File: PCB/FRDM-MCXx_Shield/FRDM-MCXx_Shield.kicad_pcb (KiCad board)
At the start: 4 copper layers, 91.4 x 54.6 mm, 92 parts, among them J2 Barrel_Jack_Switch, J3 Conn_01x04_Socket, J4 Conn_01x05_Socket, J5 Conn_01x06_Socket, M1 Motor_Servo, Q1 IRLML6401, SW1 PEC11L-4120F-N0020, SW2 SW_Push, U1 M95010-RMN6TP, U2 FXLS8974CF, U3 SHT31A-DIS, U5 SN74LV164ADR

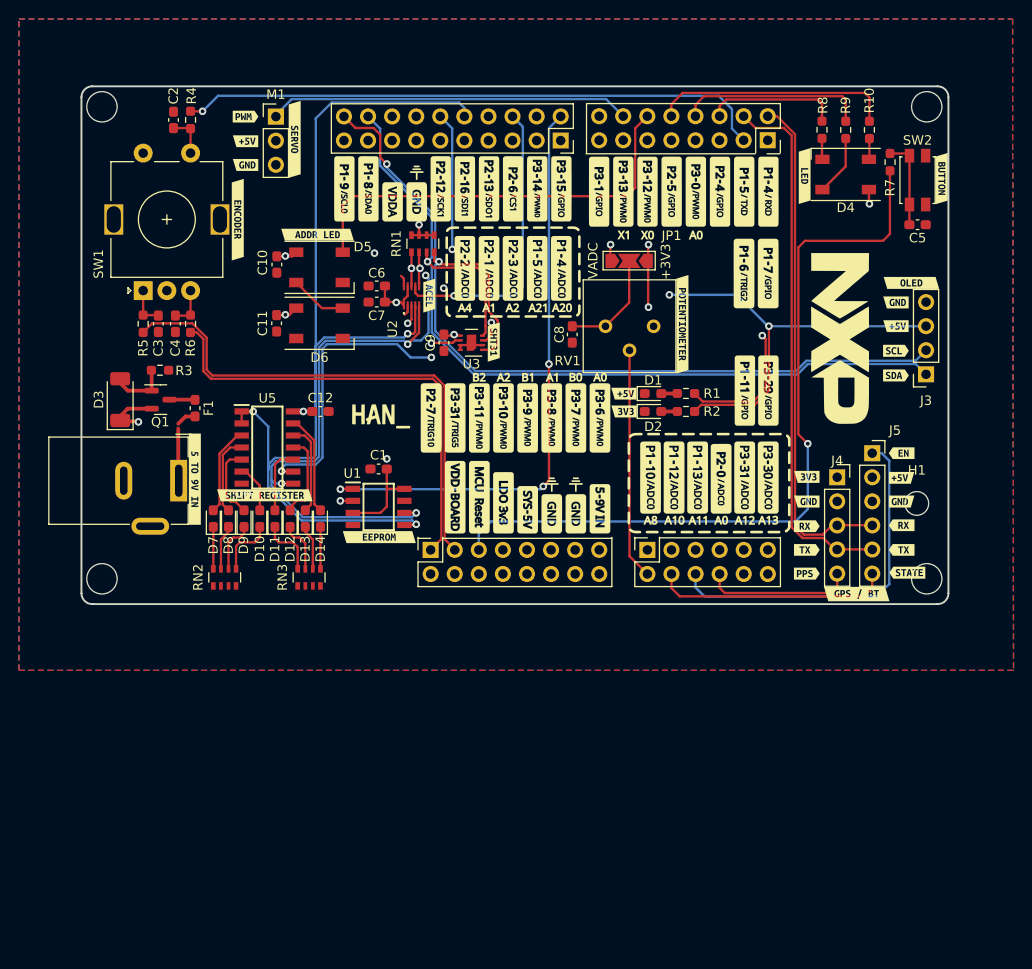
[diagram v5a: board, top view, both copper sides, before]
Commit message: Updated schematic and PCB
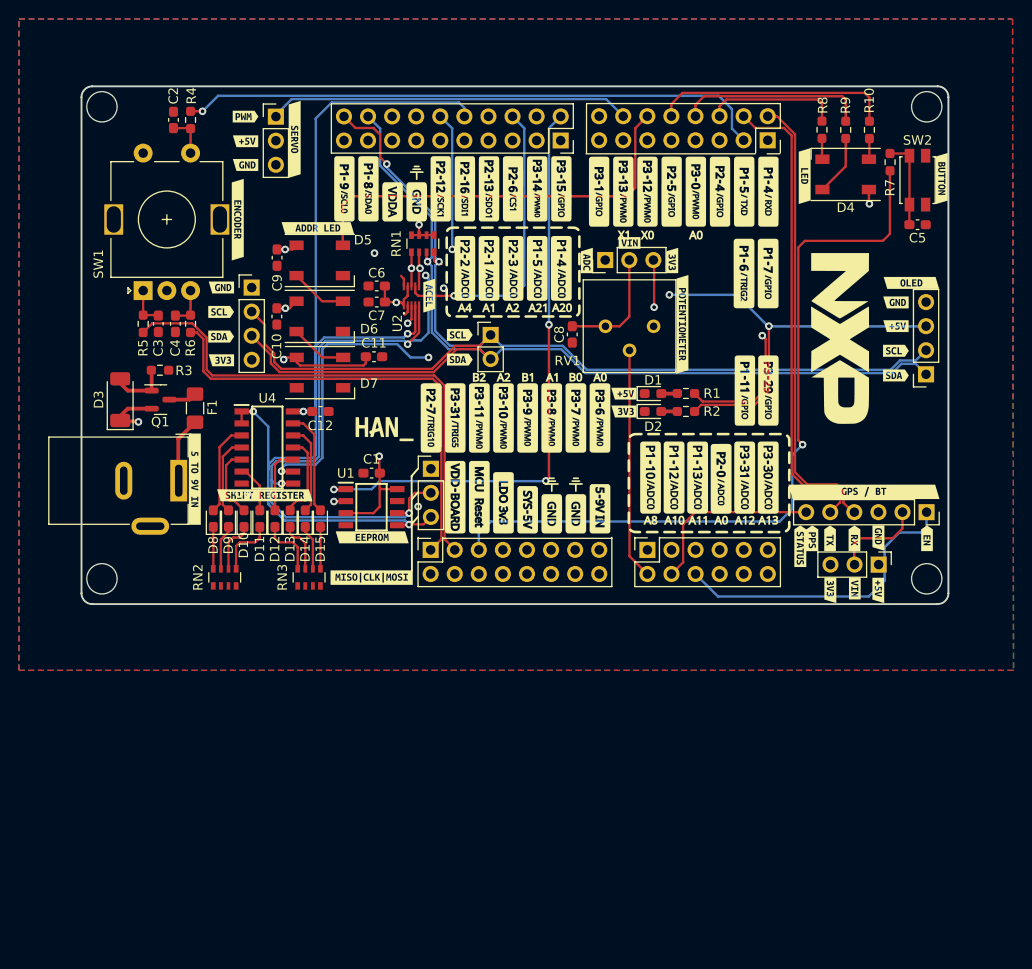
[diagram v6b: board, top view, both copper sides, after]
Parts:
- removed the C9 at (142.4, 86.2)
- removed H1: MountingHole, MountingHole:MountingHole_2.5mm
- removed U3: SHT31A-DIS, Sensor_Humidity:Sensirion_DFN-8-1EP_2.5x2.5mm_P0.5mm_EP1.1x1.7mm
- removed kibuzzard-65C7C4BF: G***, kibuzzard-65C7C4BF
- removed kibuzzard-65C7C4D7: G***, kibuzzard-65C7C4D7
- removed kibuzzard-65C7C4F7: G***, kibuzzard-65C7C4F7
- removed kibuzzard-65C7C50F: G***, kibuzzard-65C7C50F
- removed kibuzzard-65C7C529: G***, kibuzzard-65C7C529
- removed kibuzzard-65C7C54F: G***, kibuzzard-65C7C54F
- removed kibuzzard-65C7C588: G***, kibuzzard-65C7C588
- removed kibuzzard-65C7C594: G***, kibuzzard-65C7C594
- removed the kibuzzard-65C7C5A7 at (180.7, 102.9)
- removed kibuzzard-65C7C5B4: G***, kibuzzard-65C7C5B4
- removed kibuzzard-65C7CC57: G***, kibuzzard-65C7CC57
- removed kibuzzard-65C7CCCF: G***, kibuzzard-65C7CCCF
- added C11: 100nF, Capacitor_SMD:C_0603_1608Metric_Pad1.08x0.95mm_HandSolder, F.Cu at (135.1, 87.6)
- added D7: SK6812, LED_SMD:LED_SK6812_PLCC4_5.0x5.0mm_P3.2mm, F.Cu at (129.3, 89.3)
- added J2: Conn_01x03_Pin, Connector_PinHeader_2.54mm:PinHeader_1x03_P2.54mm_Vertical, F.Cu at (141.1, 99.4)
- added J3: Conn_01x02_Pin, Connector_PinHeader_2.54mm:PinHeader_1x02_P2.54mm_Vertical, F.Cu at (147.3, 85.3)
- added JP2: SolderJumper_3_Open, Connector_PinHeader_2.54mm:PinHeader_1x03_P2.54mm_Vertical, F.Cu at (188.3, 109.5)
- added kibuzzard-65C7C751: G***, kibuzzard-65C7C751, F.Cu at (118.9, 82.9)
- added kibuzzard-65C7C751: G***, kibuzzard-65C7C751, F.Cu at (144.1, 85.3)
- added kibuzzard-65C7C77A: G***, kibuzzard-65C7C77A, F.Cu at (144.1, 87.9)
- added kibuzzard-65C7C77A: G***, kibuzzard-65C7C77A, F.Cu at (118.9, 85.5)
- added kibuzzard-65D5B8C7: G***, kibuzzard-65D5B8C7, F.Cu at (188.2, 106.8)
- added kibuzzard-65D5B8D9: G***, kibuzzard-65D5B8D9, F.Cu at (185.7, 106.8)
- added kibuzzard-65D5B8E6: G***, kibuzzard-65D5B8E6, F.Cu at (183.2, 106.8)
- added kibuzzard-65D5B934: G***, kibuzzard-65D5B934, F.Cu at (183.2, 112.3)
- added kibuzzard-65D5B943: G***, kibuzzard-65D5B943, F.Cu at (188.2, 112.3)
- added kibuzzard-65D5B980: G***, kibuzzard-65D5B980, F.Cu at (181.3, 106.8)
- added kibuzzard-65D5B9E2: G***, kibuzzard-65D5B9E2, F.Cu at (185.8, 112.1)
- added kibuzzard-65D5B9E2: G***, kibuzzard-65D5B9E2, F.Cu at (162.0, 75.6)
- added kibuzzard-65D5C5A7: G***, kibuzzard-65D5C5A7, F.Cu at (180.0, 107.6)
- added kibuzzard-65D5C7B2: G***, kibuzzard-65D5C7B2, F.Cu at (119.0, 88.0)
- added kibuzzard-65D5C7BA: G***, kibuzzard-65D5C7BA, F.Cu at (119.0, 80.3)
- added kibuzzard-65D5C99D: G***, kibuzzard-65D5C99D, F.Cu at (186.7, 101.9)
- added kibuzzard-65D5CAF7: G***, kibuzzard-65D5CAF7, F.Cu at (166.5, 77.5)
- added kibuzzard-65D5CB13: G***, kibuzzard-65D5CB13, F.Cu at (157.5, 77.5)
- added kibuzzard-65D5CBEE: G***, kibuzzard-65D5CBEE, F.Cu at (134.8, 110.9)
- F1: footprint Fuse:Fuse_0603_1608Metric_Pad1.05x0.95mm_HandSolder -> Fuse:Fuse_1206_3216Metric_Pad1.42x1.75mm_HandSolder
- J4: value Conn_01x05_Socket -> Conn_01x04_Pin; footprint Connector_PinSocket_2.54mm:PinSocket_1x05_P2.54mm_Vertical -> Connector_PinHeader_2.54mm:PinHeader_1x04_P2.54mm_Vertical
- JP1: footprint Jumper:SolderJumper-3_P2.0mm_Open_TrianglePad1.0x1.5mm_NumberLabels -> Connector_PinHeader_2.54mm:PinHeader_1x03_P2.54mm_Vertical
- moved J4 64.9 mm to (122.2, 80.3)
- moved kibuzzard-65C7C6CC 9.37 mm to (193.4, 106.8), turned to -90 degrees
- moved J7 8.46 mm to (193.3, 104.0), turned to -90 degrees
- moved JP1 2.53 mm to (159.4, 77.4), turned to 90 degrees
- moved G*** 1.39 mm to (136.2, 95.2)
- moved C1 0.85 mm to (134.8, 99.9)
- moved U1 0.75 mm to (134.8, 103.5)
- moved kibuzzard-65C7CB3C 0.75 mm to (134.9, 106.7)
- moved C9 0.73 mm to (124.8, 77.2)
- moved D5 0.73 mm to (129.3, 77.5)
- moved C10 0.73 mm to (124.8, 83.4)
- moved D6 0.73 mm to (129.3, 83.4)
- moved kibuzzard-65C7CE88 0.70 mm to (129.1, 74.0)
- renumbered C11 to C10, C10 to C9, D9 to D10, D10 to D11, D11 to D12, D12 to D13, D13 to D14, D14 to D15, D7 to D8, D8 to D9, J2 to J5, J3 to J6, J5 to J7, U5 to U4
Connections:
- net /BT_STATE renamed /BT_STATE/GPS_PPS
- D6 pad 4: unconnected-(D6-DOUT-Pad4) -> Net-(D6-DOUT)
- J1 pad B7: /TEMP_ALERT -> unconnected-(J1B-P2-1/ADC0-A1-PadB7)
- J1 pad B9: /~{TEMP_RST} -> unconnected-(J1B-P2-2/ADC0-A4-PadB9)
- J1 pad C8: /GPS_PPS -> unconnected-(J1C-P2-0/ADC0-A0-PadC8)
- J4 pad 1: +3.3V -> GND
- J4 pad 2: GND -> /SCL
- J4 pad 3: /RX -> /SDA
- J4 pad 4: /TX -> +3.3V
- J7 pad 2: +5V -> Net-(J7-Pin_2)
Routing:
- net /~{TEMP_RST}: track 30.3 -> 0.00 mm, vias 1 -> 0
- net /TEMP_ALERT: track 23.4 -> 0.00 mm, vias 1 -> 0
- net +5V: track 168.7 -> 188.9 mm
- net /SCL: track 99.4 -> 116.1 mm
- net /SDA: track 95.2 -> 111.5 mm
- net /GPS_PPS: track 15.8 -> 0.00 mm
- net Net-(J7-Pin_2): track 0.00 -> 9.68 mm
- net /SPI_MISO: track 57.1 -> 66.0 mm
- net /TX: track 56.7 -> 50.0 mm
- net Net-(D6-DOUT): track 0.00 -> 6.05 mm
- net /RX: track 53.9 -> 48.0 mm
- net /BT_EN: track 37.9 -> 32.0 mm
- net /ACEL_INT1: track 62.5 -> 68.4 mm
- net /BT_STATE/GPS_PPS: track 24.9 -> 19.3 mm
- net /ACEL_INT2: track 63.5 -> 68.5 mm
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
